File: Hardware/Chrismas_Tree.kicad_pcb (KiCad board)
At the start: 2 copper layers, 264.4 x 368.3 mm, 213 parts, among them J1 DNP, J2 USB_B, Q1 DMG3414U, Q2 DMG3414U, Q3 DMG3414U, Q4 DMG3414U, U1 PIC18F23K22

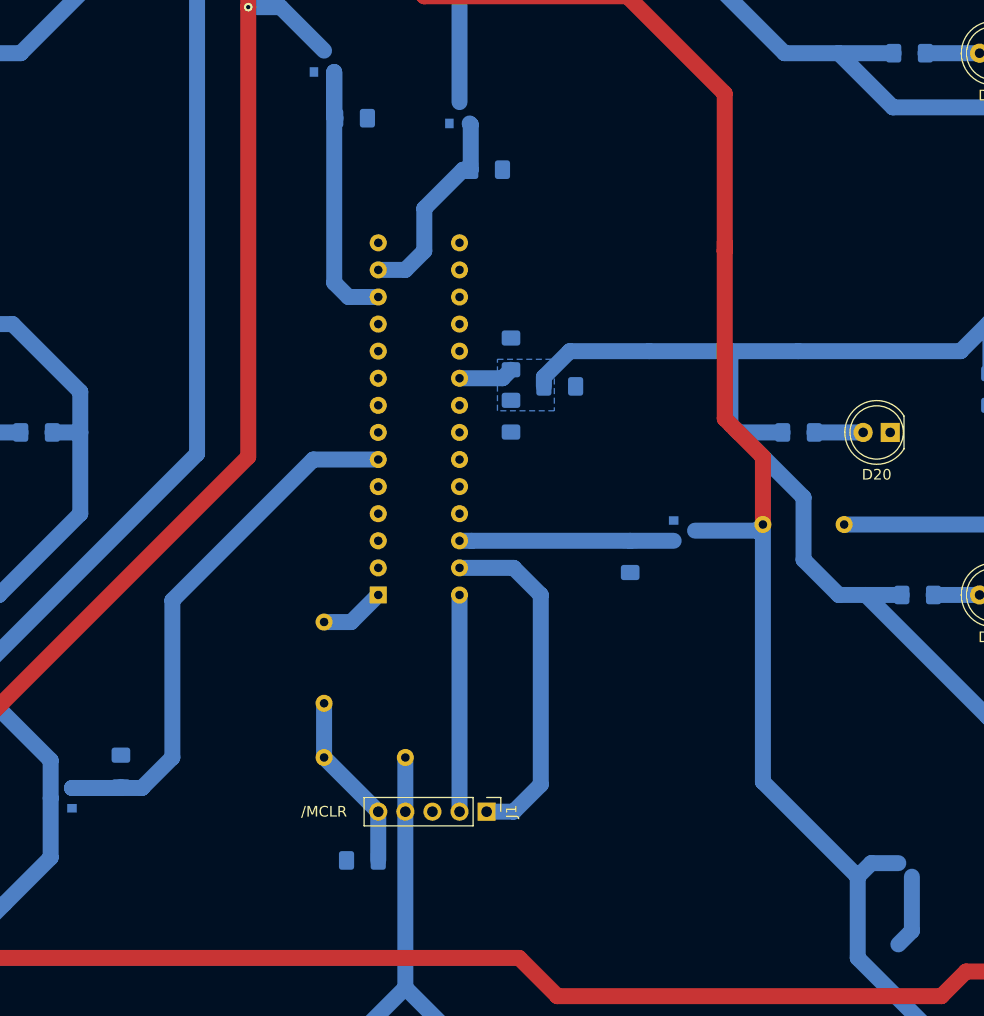
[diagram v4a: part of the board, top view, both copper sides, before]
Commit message: Changed microcontroller package for a SMD one.
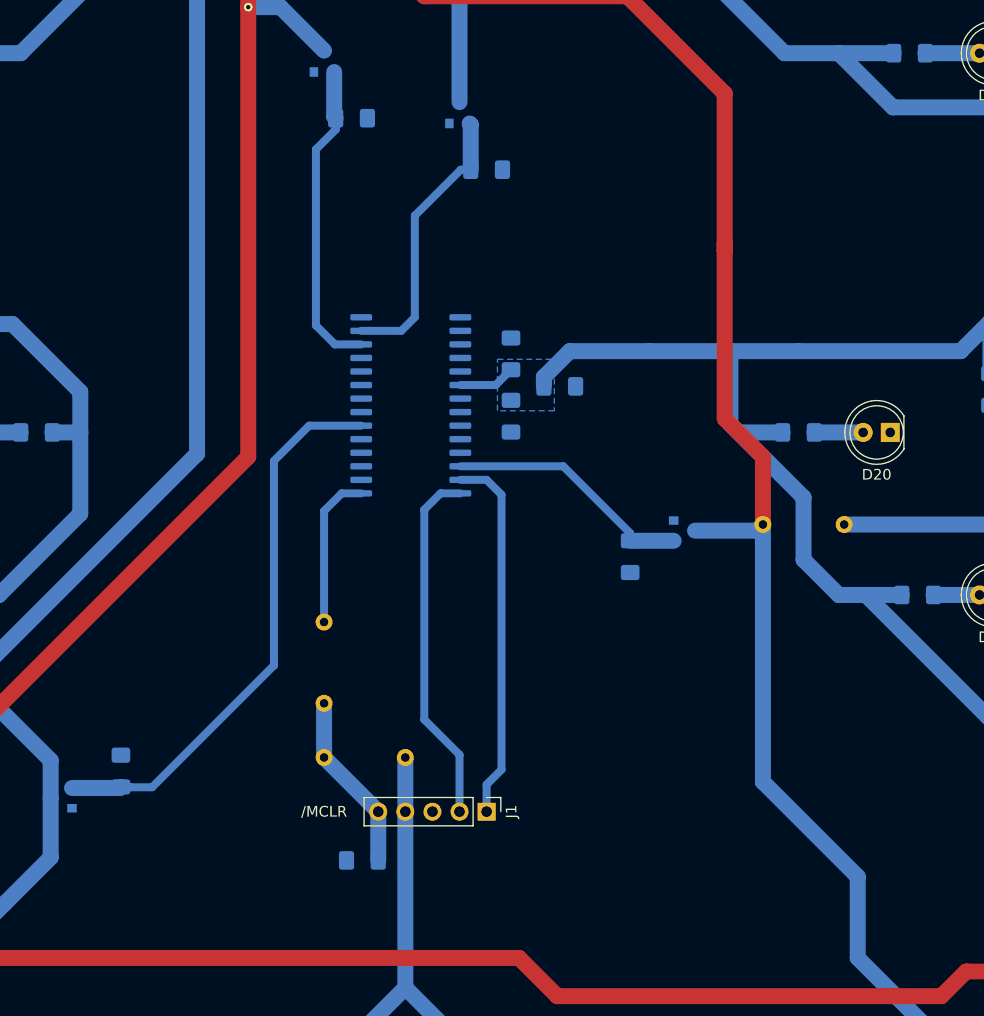
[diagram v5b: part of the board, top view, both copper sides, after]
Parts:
- U1: footprint Package_DIP:DIP-28_W7.62mm -> Package_SO:SOIC-28W_7.5x17.9mm_P1.27mm
- moved U1 18.0 mm to (161.3, 246.6)
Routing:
- net Net-(J1-Pad2): track 20.3 -> 33.7 mm
- net Net-(R97-Pad2): track 6.13 -> 14.6 mm
- net Net-(Q1-Pad1): track 19.3 -> 26.5 mm
- net GND: track 6.88 -> 0.00 mm
- net Net-(Q4-Pad3): track 218.3 -> 214.0 mm
- net Net-(Q4-Pad1): track 20.1 -> 23.3 mm
- net Net-(Q3-Pad1): track 54.7 -> 52.5 mm
- net Net-(J1-Pad1): track 32.6 -> 34.7 mm
- net Net-(Q2-Pad1): track 28.8 -> 29.6 mm
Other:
- board text added: "09/2020"
- board text removed: "11/2019"

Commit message: Added rounded corners to PCB, improved PCB dimensions to fit in millimeters.
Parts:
- moved H6 0.53 mm to (277.7, 41.0)
- moved H4 0.43 mm to (277.7, 379.0)
- moved H5 0.43 mm to (277.7, 209.8)
- moved J2 0.43 mm to (277.7, 349.2)
- moved H1 0.31 mm to (43.7, 41.0)
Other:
- board size 264.4 x 368.3 mm -> 264 x 368 mm
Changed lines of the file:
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@@
   (general
     (thickness 1.6)
-    (drawings 7)
+    (drawings 10)
     (tracks 585)
     (zones 0)
@@
   )
   (setup
-    (last_trace_width 0.75)
+    (last_trace_width 1.5)
     (user_trace_width 0.4)
     (user_trace_width 0.75)
@@
   )
   (module Connector_USB:USB_B_OST_USB-B1HSxx_Horizontal (layer B.Cu)
-    (at 278.13 349.25)
+    (at 277.702 349.25)
     (descr "USB B receptacle, Horizontal, through-hole, http://www.on-shore.com/wp-content/uploads/2015/09/usb-b1hsxx.pdf")
     (tags "USB-B receptacle horizontal through-hole")
@@
   )
   (module MountingHole:MountingHole_4.5mm_Pad (layer F.Cu)
-    (at 278.13 40.64)
+    (at 277.702 40.954)
     (descr "Mounting Hole 4.5mm")
     (tags "mounting hole 4.5mm")
@@
   )
   (module MountingHole:MountingHole_4.5mm_Pad (layer F.Cu)
-    (at 278.13 209.804)
+    (at 277.702 209.804)
     (descr "Mounting Hole 4.5mm")
     (tags "mounting hole 4.5mm")
@@
   )
   (module MountingHole:MountingHole_4.5mm_Pad (layer F.Cu)
-    (at 278.13 378.968)
+    (at 277.702 378.968)
     (descr "Mounting Hole 4.5mm")
     (tags "mounting hole 4.5mm")
@@
   )
   (module MountingHole:MountingHole_4.5mm_Pad (layer F.Cu)
-    (at 43.688 378.968)
+    (at 43.688 378.954)
     (descr "Mounting Hole 4.5mm")
     (tags "mounting hole 4.5mm")
@@
   )
   (module MountingHole:MountingHole_4.5mm_Pad (layer F.Cu)
-    (at 43.688 209.804)
+    (at 43.702 209.804)
     (descr "Mounting Hole 4.5mm")
     (tags "mounting hole 4.5mm")
@@
   )
   (module MountingHole:MountingHole_4.5mm_Pad (layer F.Cu)
-    (at 43.688 40.64)
+    (at 43.702 40.954)
     (descr "Mounting Hole 4.5mm")
     (tags "mounting hole 4.5mm")
@@
     )
   )
+  (gr_arc (start 287.702 388.954) (end 287.702 393.954) (angle -90) (layer Edge.Cuts) (width 0.05))
+  (gr_arc (start 287.702 30.954) (end 292.702 30.954) (angle -90) (layer Edge.Cuts) (width 0.05))
+  (gr_arc (start 33.702 30.954) (end 33.702 25.954) (angle -90) (layer Edge.Cuts) (width 0.05))
+  (gr_arc (start 33.702 388.954) (end 28.702 388.954) (angle -90) (layer Edge.Cuts) (width 0.05))
   (gr_text 09/2020 (at 268.224 390.398) (layer B.Mask)
     (effects (font (size 1 1) (thickness 0.15)) (justify mirror))
   )
-  (gr_line (start 28.956 393.954) (end 293.116 393.954) (layer Edge.Cuts) (width 0.05))
-  (gr_line (start 28.702 393.954) (end 28.956 393.954) (layer Edge.Cuts) (width 0.05))
-  (gr_line (start 28.702 25.654) (end 28.702 393.954) (layer Edge.Cuts) (width 0.05))
-  (gr_line (start 293.116 25.654) (end 28.702 25.654) (layer Edge.Cuts) (width 0.05))
-  (gr_line (start 293.116 393.954) (end 293.116 25.654) (layer Edge.Cuts) (width 0.05))
+  (gr_line (start 33.702 393.954) (end 287.702 393.954) (layer Edge.Cuts) (width 0.05))
+  (gr_line (start 28.702 30.954) (end 28.702 388.954) (layer Edge.Cuts) (width 0.05))
+  (gr_line (start 287.702 25.954) (end 33.702 25.954) (layer Edge.Cuts) (width 0.05))
+  (gr_line (start 292.702 388.954) (end 292.702 30.954) (layer Edge.Cuts) (width 0.05))
   (gr_text /MCLR (at 153.162 284.734) (layer F.SilkS)
     (effects (font (size 1 1) (thickness 0.15)))
@@
   (segment (start 279.4 318.77) (end 281.432 316.738) (width 1.5) (layer B.Cu) (net 83))
   (segment (start 281.432 308.864) (end 281.432 316.738) (width 1.5) (layer B.Cu) (net 83))
-  (segment (start 278.13 349.25) (end 274.32 349.25) (width 1.5) (layer B.Cu) (net 83))
   (segment (start 266.7 318.77) (end 271.78 318.77) (width 1.5) (layer B.Cu) (net 83))
   (segment (start 271.78 346.71) (end 271.78 318.77) (width 1.5) (layer B.Cu) (net 83))
-  (segment (start 274.32 349.25) (end 271.78 346.71) (width 1.5) (layer B.Cu) (net 83))
   (segment (start 271.78 318.77) (end 279.4 318.77) (width 1.5) (layer B.Cu) (net 83))
   (segment (start 172.5975 51.054) (end 176.784 46.8675) (width 1.5) (layer B.Cu) (net 83))
@@
   (segment (start 169.2545 244.729) (end 170.688 243.2955) (width 0.75) (layer B.Cu) (net 83))
   (segment (start 165.94 244.729) (end 169.2545 244.729) (width 0.75) (layer B.Cu) (net 83))
+  (segment (start 274.32 349.25) (end 277.702 349.25) (width 1.5) (layer B.Cu) (net 83))
+  (segment (start 271.78 346.71) (end 274.32 349.25) (width 1.5) (layer B.Cu) (net 83))
   (segment (start 150.622 43.434) (end 155.702 43.434) (width 1.5) (layer B.Cu) (net 84))
   (segment (start 148.336 43.434) (end 150.622 43.434) (width 1.5) (layer B.Cu) (net 84))
@@
     (polygon
       (pts
-        (xy 293.116 393.954) (xy 28.702 393.954) (xy 28.702 25.654) (xy 293.116 25.654)
+        (xy 292.702 393.954) (xy 28.702 393.954) (xy 28.702 25.954) (xy 292.702 25.954)
       )
     )
@@
     (polygon
       (pts
-        (xy 28.702 25.654) (xy 293.116 25.654) (xy 293.116 393.954) (xy 28.702 393.954)
+        (xy 28.702 25.954) (xy 292.702 25.954) (xy 292.702 393.954) (xy 28.702 393.954)
       )
     )

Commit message: Added USB connector 3D model to PCB.
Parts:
- J2: value USB_B -> 2411_06
